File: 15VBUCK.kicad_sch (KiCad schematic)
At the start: 1 part, among them U3 LM76005RNPR

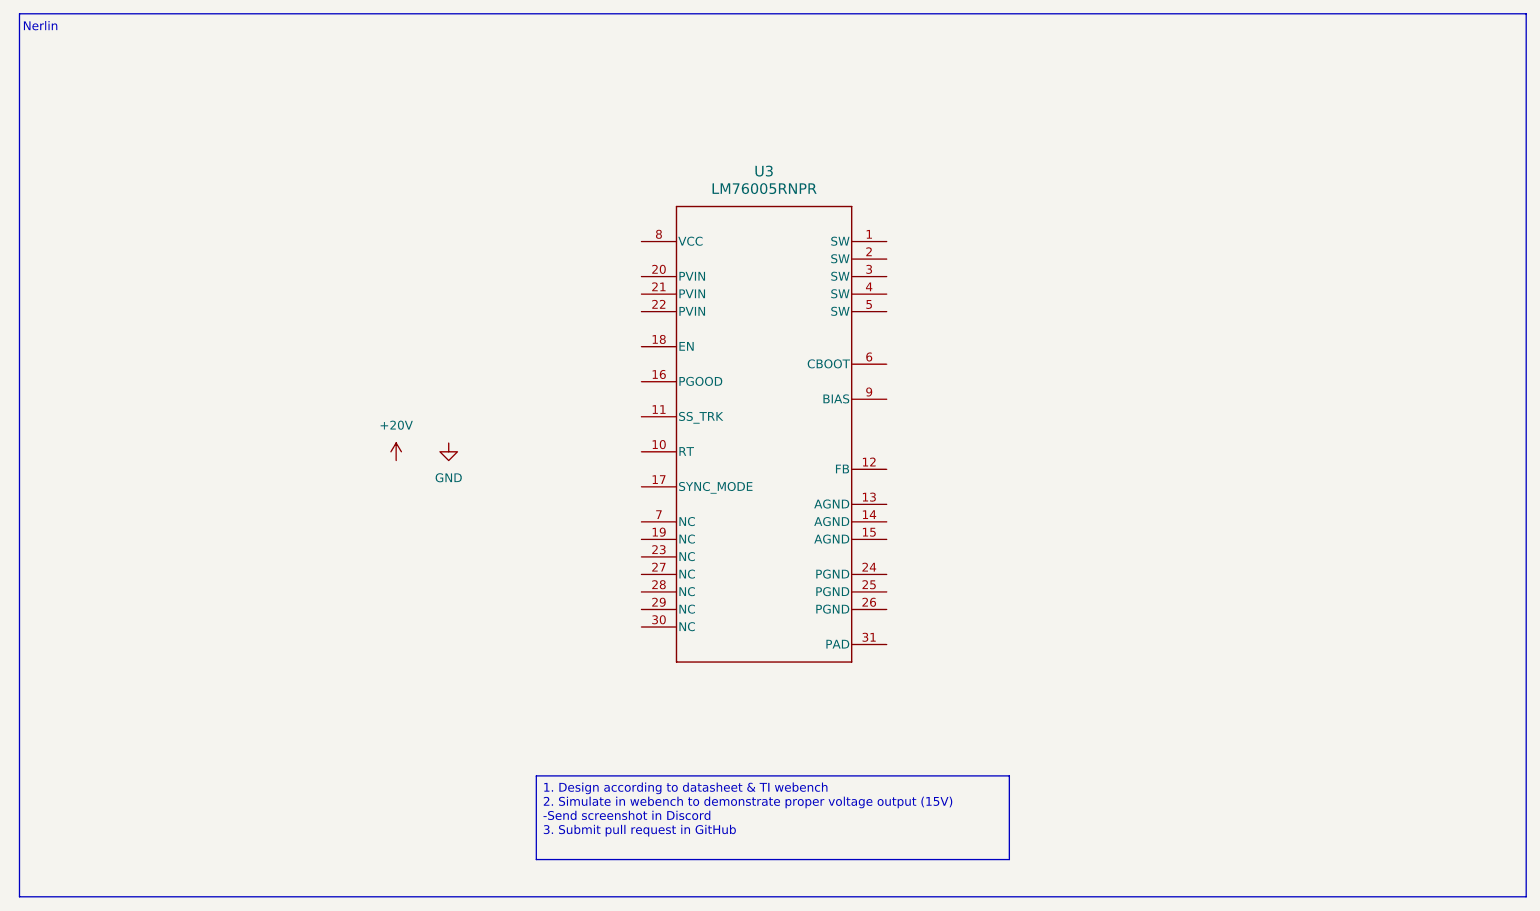
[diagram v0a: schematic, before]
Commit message: Schematic for 15v Buck
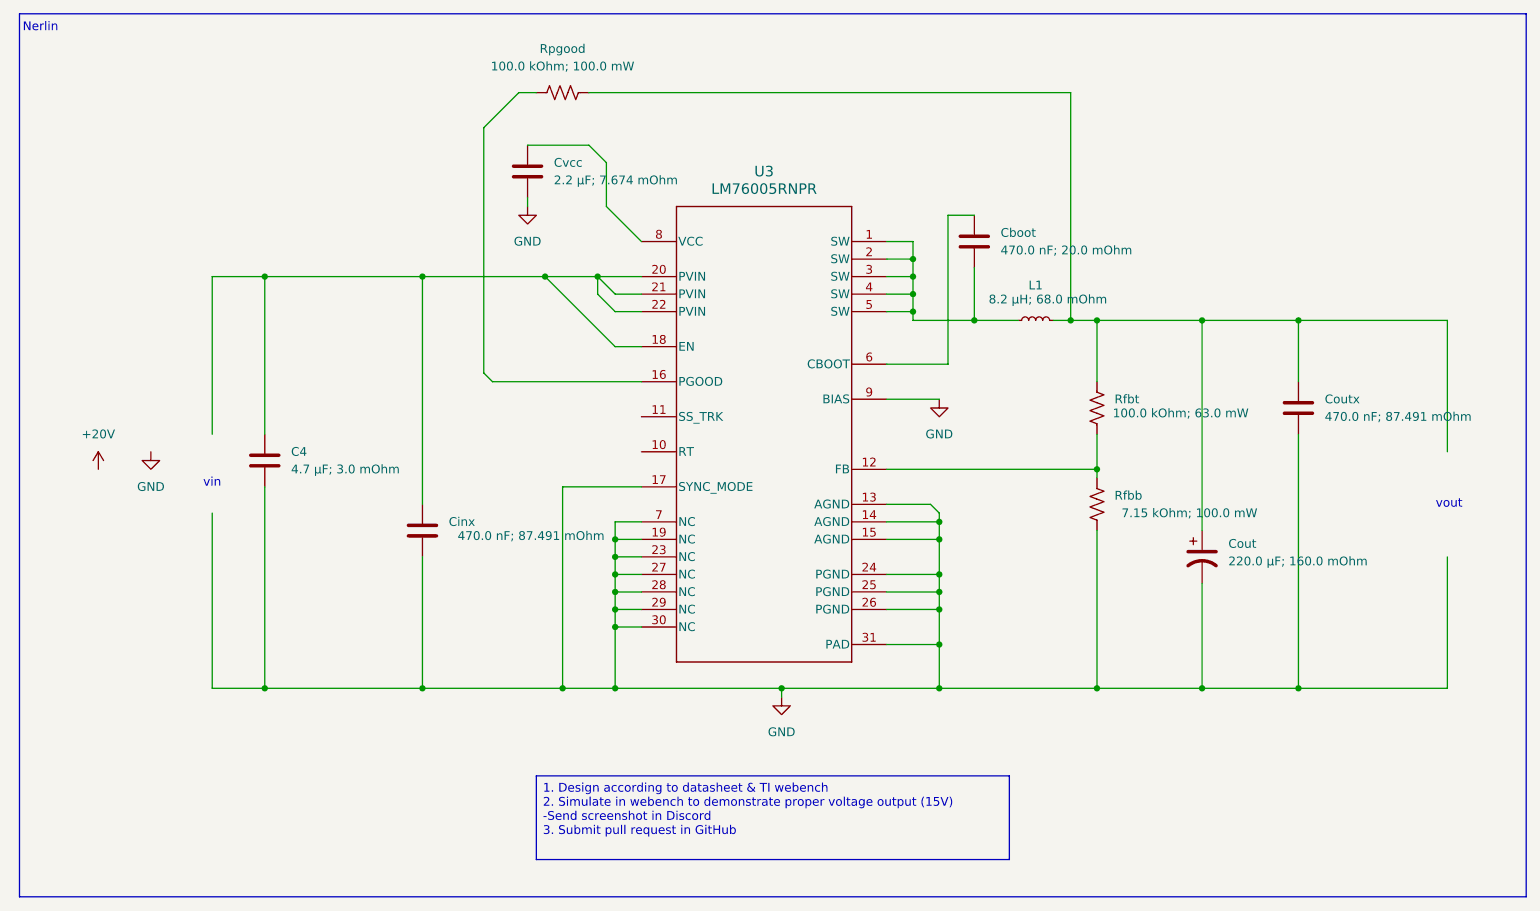
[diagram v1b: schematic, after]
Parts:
- added C4: 4.7 µF; 3.0 mOhm, symbol Device:C
- added Cboot: 470.0 nF; 20.0 mOhm, symbol Device:C
- added Cinx, Coutx: 470.0 nF; 87.491 mOhm, symbol Device:C
- added Cout: 220.0 μF; 160.0 mOhm, symbol Device:C_Polarized_US
- added Cvcc: 2.2 μF; 7.674 mOhm, symbol Device:C
- added L1: 8.2 μH; 68.0 mOhm, symbol Device:L_Small
- added Rfbb: 7.15 kOhm; 100.0 mW, symbol Device:R_US
- added Rfbt: 100.0 kOhm; 63.0 mW, symbol Device:R_US
- added Rpgood: 100.0 kOhm; 100.0 mW, symbol Device:R_US
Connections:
- net GND: now also U3.13 (AGND), U3.14 (AGND), U3.15 (AGND), U3.17 (SYNC_MODE), U3.19 (NC), U3.23 (NC), U3.24 (PGND), U3.25 (PGND), U3.26 (PGND), U3.27 (NC), U3.28 (NC), U3.29 (NC), U3.30 (NC), U3.31 (PAD), U3.7 (NC), U3.9 (BIAS), C4.2, Cinx.2, Cout.2, Coutx.2, Cvcc.2, Rfbb.1
- net at U3.1 (SW): now also U3.2 (SW), U3.3 (SW), U3.4 (SW), U3.5 (SW), Cboot.2, L1.1
- net at U3.12 (FB): now also Rfbb.2, Rfbt.1
- net at U3.16 (PGOOD): now also Rpgood.1
- net at U3.18 (EN): now also U3.20 (PVIN), U3.21 (PVIN), U3.22 (PVIN), C4.1, Cinx.1
- net at U3.6 (CBOOT): now also Cboot.1
- net at U3.8 (VCC): now also Cvcc.1
- new net: Cout.1, Coutx.1, L1.2, Rfbt.2, Rpgood.2
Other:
- note added: "vin"
- note added: "vout"
